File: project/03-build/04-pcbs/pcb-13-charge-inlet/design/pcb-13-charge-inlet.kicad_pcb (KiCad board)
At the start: 2 copper layers, 28 x 15 mm, 0 parts

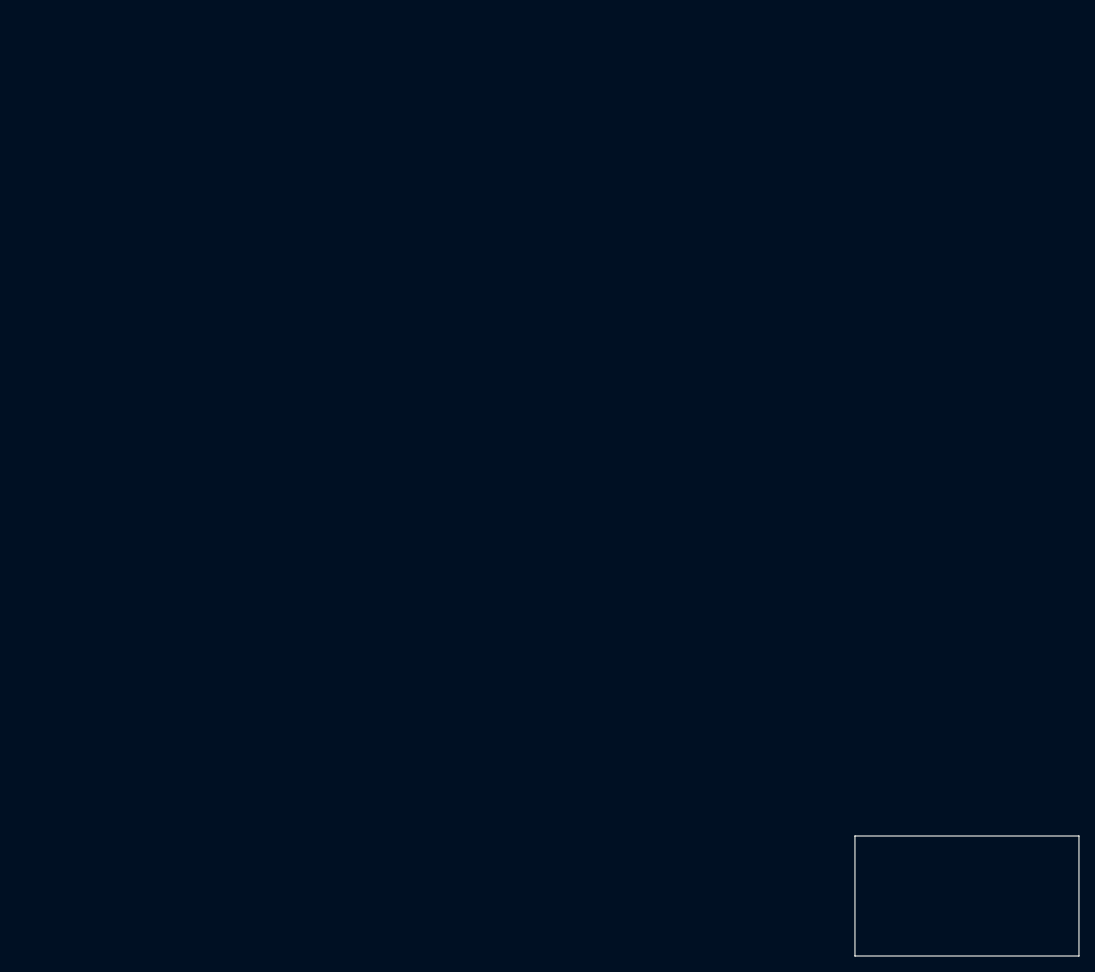
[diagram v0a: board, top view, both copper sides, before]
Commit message: build(pcbs): PCB-13 placed and routed (lesson 4); DRC 0 errors, 0 unconnected, parity clean
Hand-routed, octolinear, two layers at 1 oz. 3 A path as pours: VBUS 2.41 mm narrowest,
VSNK 1.29 mm past H2. D-069 amended at placement: ADDR0/ADDR1/RESET to GND (R5-R7 out),
TP5-TP8 out, D2 inputs swapped, J2 turned 180. New playbook traps: KiPy is_rule_area()
is a method; plan a crowded QFN's orientation first.

Co-Authored-By: Claude Opus 5.5 <noreply@anthropic.com>
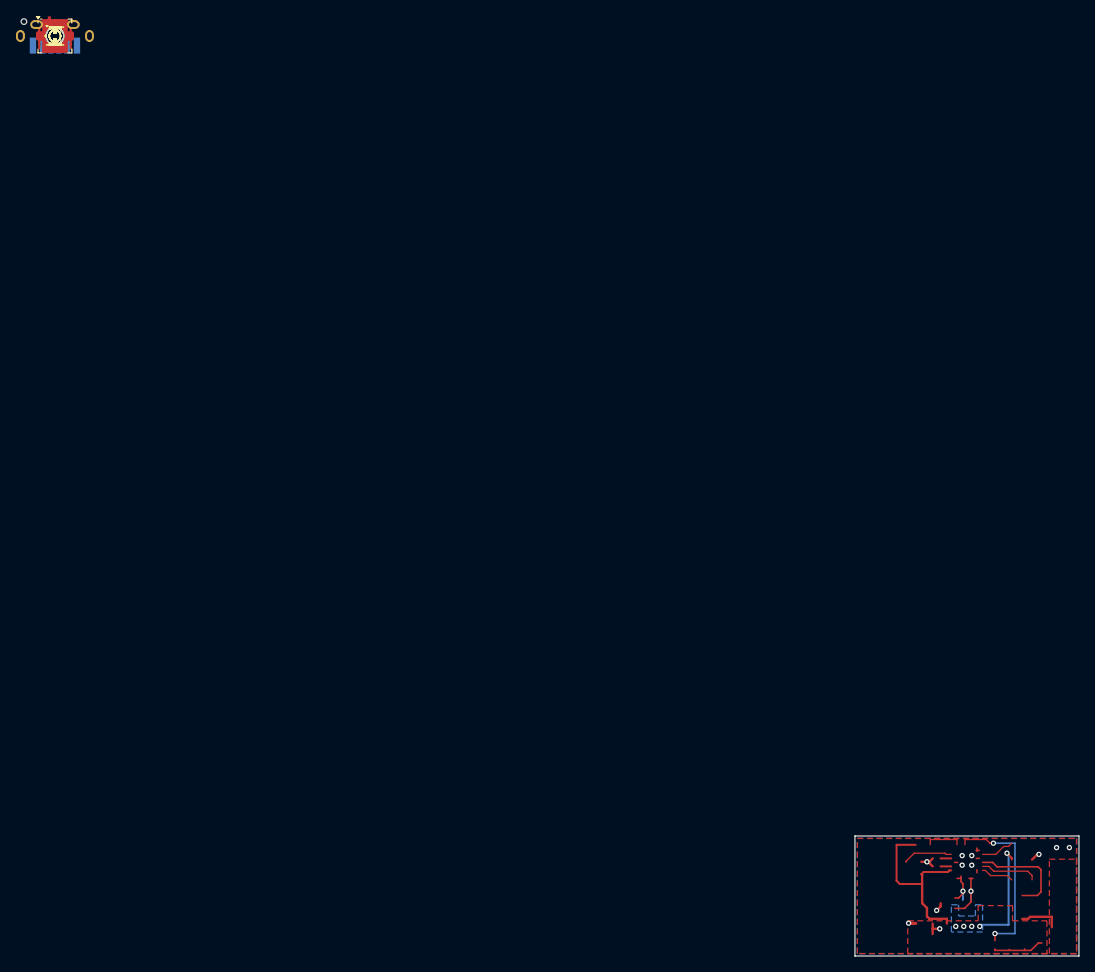
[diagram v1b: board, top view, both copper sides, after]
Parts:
- added C1: 4.7u 50V, Capacitor_SMD:C_1206_3216Metric, F.Cu at (0.00, 0.00)
- added C2: 1u 50V, Capacitor_SMD:C_0603_1608Metric, F.Cu at (0.00, 0.00)
- added C3, C4: 1u 10V, Capacitor_SMD:C_0402_1005Metric, F.Cu at (0.00, 0.00)
- added C5: 100n 50V, Capacitor_SMD:C_0603_1608Metric, F.Cu at (0.00, 0.00)
- added D1: TVS2200DRV, Package_SON:WSON-6-1EP_2x2mm_P0.65mm_EP1x1.6mm, F.Cu at (0.00, 0.00)
- added D2: ESDA25W, Package_TO_SOT_SMD:SOT-323_SC-70, F.Cu at (0.00, 0.00)
- added H1, H2: M2, MountingHole:MountingHole_2.2mm_M2, F.Cu at (0.00, 0.00)
- added J1: USB4140-GF-0170-C, pcb13:GCT_USB4140-GF-0170-C, B.Cu at (0.00, 0.00)
- added J2: W16 pads, pcb13:W16_SolderPads_2x_AWG22, F.Cu at (0.00, 0.00)
- added Q1: STL6P3LLH6, pcb13:ST_PowerFLAT-3.3x3.3_TypeF, F.Cu at (0.00, 0.00)
- added R1: 1k, Resistor_SMD:R_0805_2012Metric, F.Cu at (0.00, 0.00)
- added R2: 470, Resistor_SMD:R_1206_3216Metric, F.Cu at (0.00, 0.00)
- added R3: 100k, Resistor_SMD:R_0402_1005Metric, F.Cu at (0.00, 0.00)
- added R4: 33k, Resistor_SMD:R_0402_1005Metric, F.Cu at (0.00, 0.00)
- added TP1: VBUS, TestPoint:TestPoint_Pad_D1.0mm, F.Cu at (0.00, 0.00)
- added TP10: POWER_OK2, TestPoint:TestPoint_Pad_D1.0mm, F.Cu at (0.00, 0.00)
- added TP2: GND, TestPoint:TestPoint_Pad_D1.0mm, F.Cu at (0.00, 0.00)
- added TP3: SCL, TestPoint:TestPoint_Pad_D1.0mm, F.Cu at (0.00, 0.00)
- added TP4: SDA, TestPoint:TestPoint_Pad_D1.0mm, F.Cu at (0.00, 0.00)
- added TP9: ATTACH, TestPoint:TestPoint_Pad_D1.0mm, F.Cu at (0.00, 0.00)
- added U1: STUSB4500QTR, Package_DFN_QFN:QFN-24-1EP_4x4mm_P0.5mm_EP2.7x2.7mm, F.Cu at (0.00, 0.00)
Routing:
- net /VBUS: track 0.00 -> 36.6 mm, vias 0 -> 5
- net /EN_SNK: track 0.00 -> 21.8 mm, vias 0 -> 2
- net /DISCH: track 0.00 -> 13.0 mm
- net /GND: track 0.00 -> 9.65 mm, vias 0 -> 11
- net /SDA: track 0.00 -> 7.20 mm
- net /CC2: track 0.00 -> 6.89 mm, vias 0 -> 1
- net /GATE: track 0.00 -> 6.76 mm
- net /POWER_OK2: track 0.00 -> 6.26 mm
- net /CC1: track 0.00 -> 5.13 mm, vias 0 -> 1
- net /VSNK: track 0.00 -> 5.11 mm
- net /VS_DISCH: track 0.00 -> 4.66 mm
- net /ATTACH: track 0.00 -> 4.22 mm
- net /SCL: track 0.00 -> 4.13 mm
- net /VREG_2V7: track 0.00 -> 1.36 mm
- net /VREG_1V2: track 0.00 -> 1.36 mm
- added copper zone on B.Cu, net /GND
- added copper zone on F.Cu, net /GND
- added copper zone on B.Cu, net /VBUS
- added copper zone on F.Cu, net /VBUS
- added copper zone on F.Cu, net /VSNK
